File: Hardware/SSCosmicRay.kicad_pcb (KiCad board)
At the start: 2 copper layers, 80 x 50 mm, 139 parts, among them J2 USB_MINI, J3 CONN-9, SW1 PGM, SW2 RST, U1 MAX4477, U2 MAX4477, U3 MAX4477, U4 MAX4477, U5 MAX4477, U7 LTC3129-SOP, U8 AOZ1280, X1 8MHz

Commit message: Update components
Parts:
- removed D17: CDBA140, SODFL5126-N
- removed J2: USB_MINI, CONN-WURTH-651005136421
- removed R12, R18, R19: 10k, RESC1608-N
- removed SW1: PGM, SW-TL3315
- removed SW2: RST, SW-TL3315
- added J1: ICSP-CORTEX, CONN-TC-2030-NL, F.Cu at (219.5, 94.0)
- added U6: STM32L100RBT6, QFP50P1200X1200-64N, F.Cu at (231.0, 69.5)
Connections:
- C17 pad 2: GND -> (no net)
- C18 pad 1: +3.3V -> (no net)
- C18 pad 2: GND -> (no net)
- C20 pad 1: +3.3V -> (no net)
- C20 pad 2: GND -> (no net)
- C21 pad 2: GND -> (no net)
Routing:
- net /Processor/MCLR: track 15.2 -> 0.00 mm
- net GND: track 164.7 -> 151.4 mm, vias 56 -> 55
- net +3.3V: track 48.7 -> 35.8 mm
- net /Processor/PGM: track 10.2 -> 0.00 mm
- net (no net): track 10.1 -> 6.46 mm, vias 0 -> 1

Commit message: Processor support circuitry
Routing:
- net /Processor/A2: track 29.2 -> 4.41 mm
- net /Processor/A1: track 28.0 -> 4.53 mm
- net /Processor/OSC2: track 10.8 -> 0.00 mm
- net /Processor/OSC1: track 10.8 -> 0.00 mm
- net (no net): track 6.46 -> 0.00 mm, vias 1 -> 0
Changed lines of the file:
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@@
   (general
     (links 246)
-    (no_connects 15)
-    (area 126.949999 52.949999 207.050001 103.050001)
+    (no_connects 17)
+    (area 116.000001 48.04 238.500422 108.7)
     (thickness 1.6)
     (drawings 44)
-    (tracks 598)
+    (tracks 572)
     (zones 0)
     (modules 134)
@@
     (effects (font (size 1.5 1.5) (thickness 0.3)))
   )
-  (segment (start 184 76.67) (end 184 77.5) (width 0.2032) (layer F.Cu) (net 0))
-  (segment (start 183.2 78.3) (end 183.2 79) (width 0.2032) (layer F.Cu) (net 0))
-  (segment (start 184 77.5) (end 183.2 78.3) (width 0.2032) (layer F.Cu) (net 0))
-  (segment (start 184.8 76.67) (end 184.8 75.2) (width 0.2032) (layer F.Cu) (net 0))
-  (via (at 184.8 75.2) (size 0.889) (layers F.Cu B.Cu) (net 0))
-  (segment (start 184.8 76.67) (end 184.8 79) (width 0.2032) (layer F.Cu) (net 0))
   (segment (start 140.3 99) (end 141.5 99) (width 0.2032) (layer B.Cu) (net 1))
   (segment (start 141.5 99) (end 140.3 99) (width 0.2032) (layer F.Cu) (net 1))
@@
   (segment (start 166.2 91.6) (end 166.2 90) (width 0.2032) (layer F.Cu) (net 13))
   (segment (start 166.85 92.25) (end 166.2 91.6) (width 0.2032) (layer F.Cu) (net 13))
-  (segment (start 160 78) (end 179.7 78) (width 0.2032) (layer F.Cu) (net 14))
-  (segment (start 159.675 77.675) (end 160 78) (width 0.2032) (layer F.Cu) (net 14))
-  (segment (start 159.675 75.835) (end 159.675 77.675) (width 0.2032) (layer F.Cu) (net 14))
-  (segment (start 180 77.7) (end 180 76.67) (width 0.2032) (layer F.Cu) (net 14))
-  (segment (start 179.7 78) (end 180 77.7) (width 0.2032) (layer F.Cu) (net 14))
   (segment (start 159.2 73.5) (end 159.2 71.5) (width 0.2032) (layer F.Cu) (net 14))
   (segment (start 159.675 75.835) (end 159.675 74.675) (width 0.2032) (layer F.Cu) (net 14))
   (segment (start 159.2 74.2) (end 159.2 73.5) (width 0.2032) (layer F.Cu) (net 14))
   (segment (start 159.675 74.675) (end 159.2 74.2) (width 0.2032) (layer F.Cu) (net 14))
-  (segment (start 159.5 78.5) (end 180.5 78.5) (width 0.2032) (layer F.Cu) (net 15))
-  (segment (start 159.025 80.165) (end 159.025 78.975) (width 0.2032) (layer F.Cu) (net 15))
-  (segment (start 159.5 78.5) (end 159.025 78.975) (width 0.2032) (layer F.Cu) (net 15))
-  (segment (start 180.8 78.2) (end 180.8 76.67) (width 0.2032) (layer F.Cu) (net 15))
-  (segment (start 180.5 78.5) (end 180.8 78.2) (width 0.2032) (layer F.Cu) (net 15))
   (segment (start 159.2 82.5) (end 159.2 84.5) (width 0.2032) (layer F.Cu) (net 15))
   (segment (start 159.2 82.5) (end 159.2 81.7) (width 0.2032) (layer F.Cu) (net 15))
   (segment (start 159.025 81.525) (end 159.025 80.165) (width 0.2032) (layer F.Cu) (net 15))
   (segment (start 159.2 81.7) (end 159.025 81.525) (width 0.2032) (layer F.Cu) (net 15))
-  (segment (start 183.85 82) (end 185.6 82) (width 0.2032) (layer F.Cu) (net 16))
-  (segment (start 185.6 76.67) (end 185.6 82) (width 0.2032) (layer F.Cu) (net 16))
-  (segment (start 185.6 82) (end 185.6 84.8) (width 0.2032) (layer F.Cu) (net 16))
-  (segment (start 185.4 85) (end 184.8 85) (width 0.2032) (layer F.Cu) (net 16))
-  (segment (start 185.6 84.8) (end 185.4 85) (width 0.2032) (layer F.Cu) (net 16))
-  (segment (start 188.15 82) (end 186.4 82) (width 0.2032) (layer F.Cu) (net 17))
-  (segment (start 186.4 76.67) (end 186.4 82) (width 0.2032) (layer F.Cu) (net 17))
-  (segment (start 186.4 82) (end 186.4 84.8) (width 0.2032) (layer F.Cu) (net 17))
-  (segment (start 186.6 85) (end 187.2 85) (width 0.2032) (layer F.Cu) (net 17))
-  (segment (start 186.4 84.8) (end 186.6 85) (width 0.2032) (layer F.Cu) (net 17))
   (segment (start 167.84 95.75) (end 166.85 95.75) (width 0.2032) (layer F.Cu) (net 18))
   (via (at 166.45 95.25) (size 0.889) (layers F.Cu B.Cu) (net 18))

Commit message: Rough layout processor support components
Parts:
- added C47: 0.1uF, CAPC1608-N, F.Cu at (233.0, 77.5)
- added C48: 1uF, CAPC1608-N, F.Cu at (233.0, 79.5)
- added C49: 0.1uF, CAPC1608-N, F.Cu at (233.0, 81.5)
- added C50: 0.1uF, CAPC1608-N, F.Cu at (223.0, 73.0)
- added C51: 0.1uF, CAPC1608-N, F.Cu at (227.5, 77.5)
- added FB1: FERRITE, INDC1608-N, F.Cu at (236.0, 78.5)
- added R12: 10k, RESC1608-N, F.Cu at (221.0, 73.0)
- added R18: 10k, RESC1608-N, F.Cu at (227.5, 79.5)
- C17, C36, C39, C43, C44: footprint CAPC1608-N -> CAPC2012-N
- moved C17 57.0 mm to (238.5, 78.5), turned to 270 degrees
- moved C18 55.4 mm to (239.0, 72.5), turned to 270 degrees
- moved C21 52.3 mm to (227.5, 61.5), turned to 0 degrees
- moved C20 47.2 mm to (239.0, 66.0)
- moved J1 28.0 mm to (220.5, 66.0), turned to 270 degrees
- moved C43 0.50 mm to (173.0, 97.5)
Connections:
- C16 pad 1: /Processor/OSC1 -> /Processor/OSCI
- C17 pad 1: (no net) -> +3.3V
- C17 pad 2: (no net) -> GND
- C18 pad 1: (no net) -> +3.3V
- C18 pad 2: (no net) -> GND
- C19 pad 1: /Processor/OSC2 -> /Processor/OSCO
- C20 pad 1: (no net) -> +3.3V
- C20 pad 2: (no net) -> GND
- C21 pad 1: (no net) -> +3.3V
- C21 pad 2: (no net) -> GND
- J1 pad 2: (no net) -> /Processor/SWDIO
- J1 pad 3: (no net) -> /Processor/~RST
- J1 pad 4: (no net) -> /Processor/SWCLK
- U6 pad 1: (no net) -> /Processor/VLCD
- U6 pad 12: (no net) -> GND
- U6 pad 13: (no net) -> +3.3VADC
- U6 pad 18: (no net) -> GND
- U6 pad 19: (no net) -> +3.3V
- U6 pad 31: (no net) -> GND
- U6 pad 32: (no net) -> +3.3V
- U6 pad 46: (no net) -> /Processor/SWDIO
- U6 pad 47: (no net) -> GND
- U6 pad 48: (no net) -> +3.3V
- U6 pad 49: (no net) -> /Processor/SWCLK
- U6 pad 5: (no net) -> /Processor/OSCI
- U6 pad 6: (no net) -> /Processor/OSCO
- U6 pad 60: (no net) -> /Processor/BOOT
- U6 pad 63: (no net) -> GND
- U6 pad 64: (no net) -> +3.3V
- U6 pad 7: (no net) -> /Processor/~RST
- X1 pad 1: /Processor/OSC1 -> /Processor/OSCI
- X1 pad 2: /Processor/OSC2 -> /Processor/OSCO
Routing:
- net +12V: track 11.7 -> 10.4 mm, vias 5 -> 2

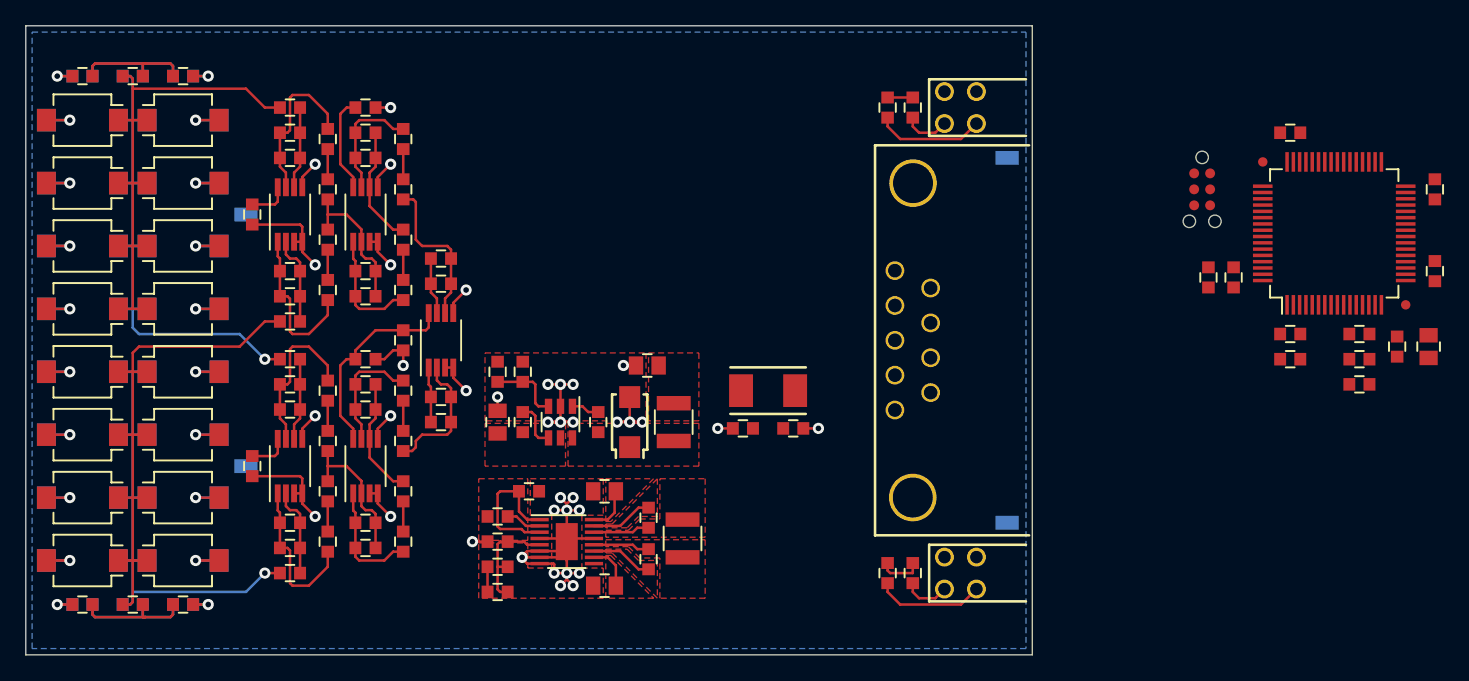
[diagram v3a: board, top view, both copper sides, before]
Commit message: Add threshold detector
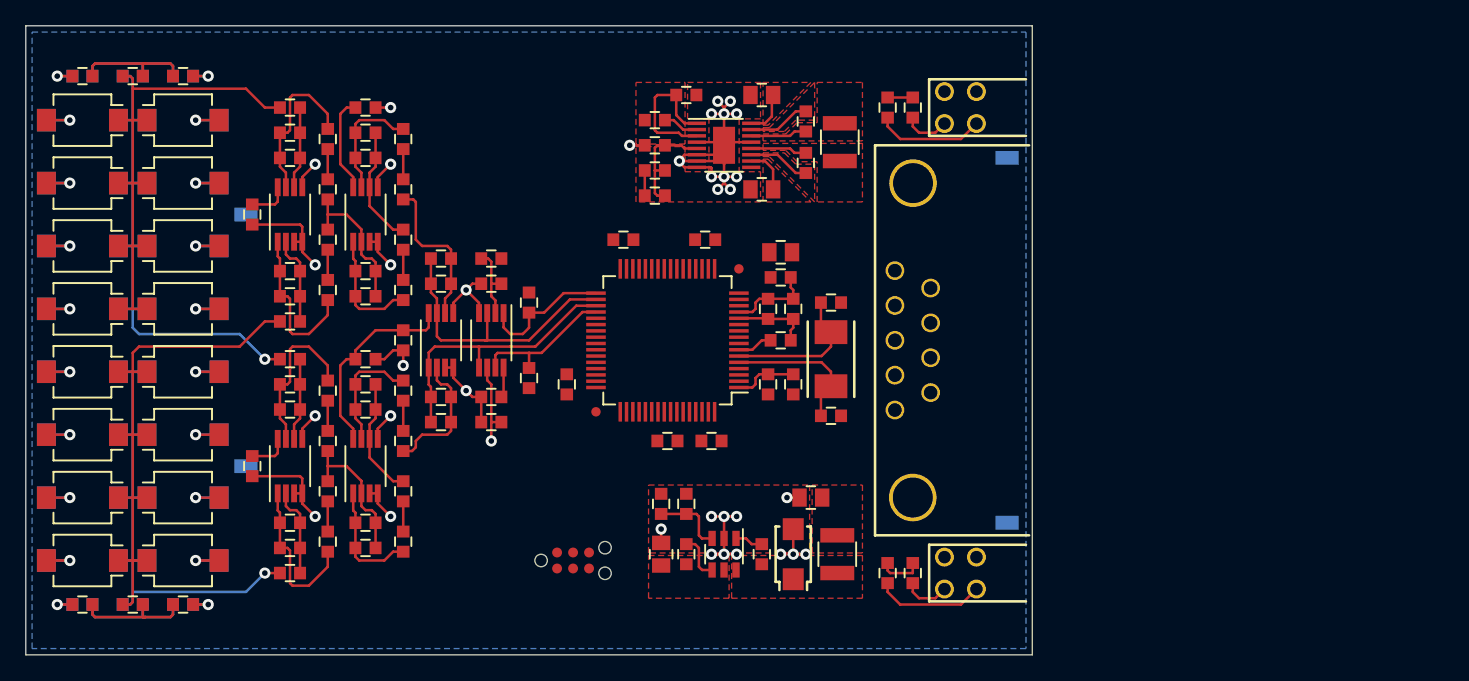
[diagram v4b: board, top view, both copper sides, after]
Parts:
- added C52: 0.1uF, CAPC1608-N, F.Cu at (164.0, 82.5)
- added C53: 0.1uF, CAPC1608-N, F.Cu at (164.0, 73.5)
- added C54: 0.1uF, CAPC1608-N, F.Cu at (164.0, 84.5)
- added R19: 10k, RESC1608-N, F.Cu at (164.0, 71.5)
- added R21: 10k, RESC1608-N, F.Cu at (167.0, 75.0)
- added R41: 10k, RESC1608-N, F.Cu at (167.0, 81.0)
- added U9: LM2903DT, SOP65P490-8N, F.Cu at (164.0, 78.0)
- moved C20 64.6 mm to (174.5, 70.0), turned to 0 degrees
- moved C21 60.9 mm to (170.0, 81.5), turned to 90 degrees
- moved J1 58.1 mm to (170.5, 95.5), turned to 0 degrees
- moved C18 58.1 mm to (181.0, 70.0), turned to 0 degrees
- moved U6 53.7 mm to (178.0, 78.0), turned to 90 degrees
- moved C17 52.0 mm to (187.0, 71.0), turned to 0 degrees
- moved FB1 49.3 mm to (187.0, 73.0), turned to 180 degrees
- moved C47 47.0 mm to (186.0, 75.5), turned to 270 degrees
- moved C49 46.1 mm to (187.0, 78.0)
- moved C48 45.2 mm to (188.0, 75.5), turned to 270 degrees
- moved R12 44.9 mm to (178.0, 86.0), turned to 0 degrees
- moved C50 43.5 mm to (181.5, 86.0), turned to 180 degrees
- moved C51 41.7 mm to (186.0, 81.5), turned to 270 degrees
- moved R18 39.6 mm to (188.0, 81.5), turned to 270 degrees
- moved C40 33.9 mm to (189.0, 63.9)
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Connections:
- J3 pad 7: (no net) -> /Processor/AOut
- U6 pad 20: (no net) -> /Processor/AOut
- U6 pad 21: (no net) -> /Processor/ATHR
- U6 pad 33: (no net) -> /Processor/DET1
- U6 pad 34: (no net) -> /Processor/A1
- U6 pad 35: (no net) -> /Processor/A2
- U6 pad 36: (no net) -> /Processor/DET2
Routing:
- net /Processor/A1: track 4.53 -> 22.8 mm
- net /Processor/A2: track 4.41 -> 22.1 mm
- net /Processor/THRSH: track 0.00 -> 12.7 mm, vias 0 -> 1
- net /Processor/DET2: track 0.00 -> 11.6 mm
- net /Processor/OSCO: track 0.00 -> 11.5 mm
- net /Processor/OSCI: track 0.00 -> 11.5 mm
- net GND: track 151.4 -> 162.2 mm, vias 55 -> 53
- net /Processor/DET1: track 0.00 -> 10.8 mm
- net +3.3VADC: track 0.00 -> 6.83 mm
- net /Processor/VLCD: track 0.00 -> 5.05 mm
- net /Processor/~RST: track 0.00 -> 2.83 mm
- net +3.3V: track 35.8 -> 38.2 mm

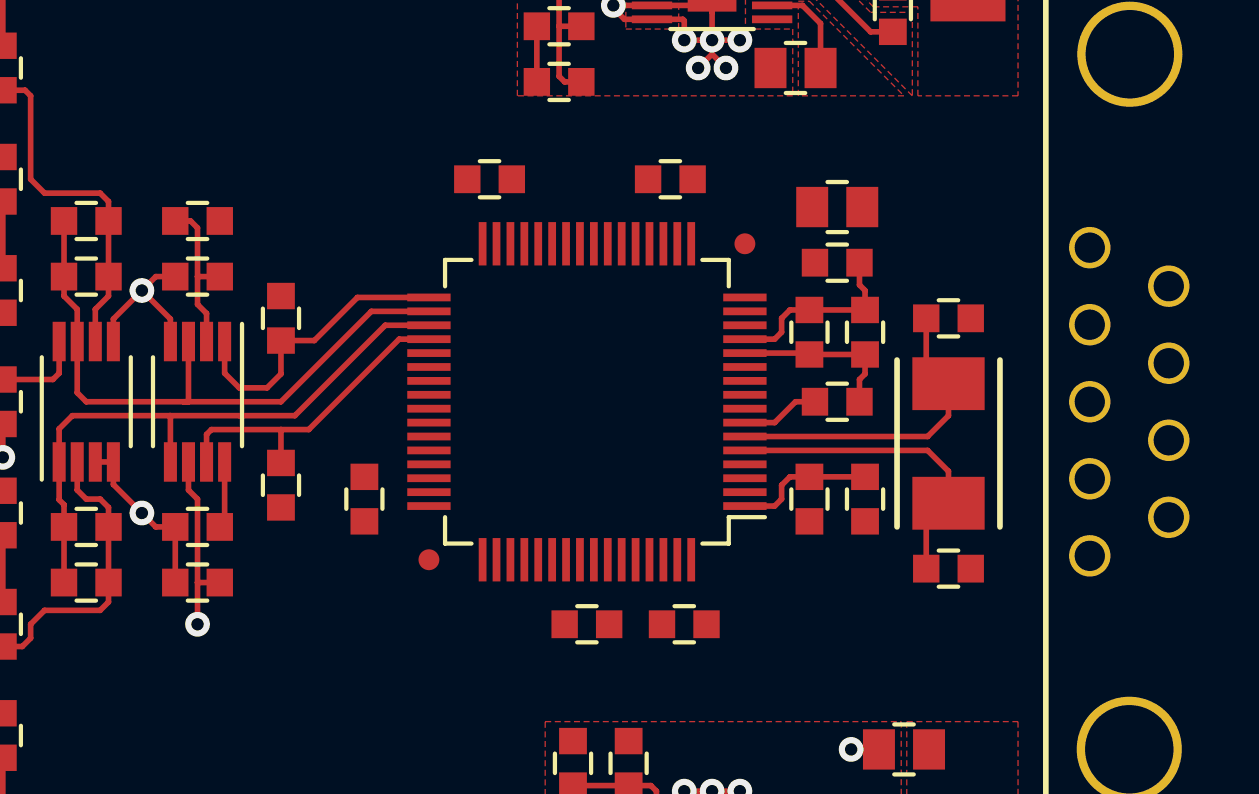
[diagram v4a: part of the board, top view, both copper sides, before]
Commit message: Serial IO connections
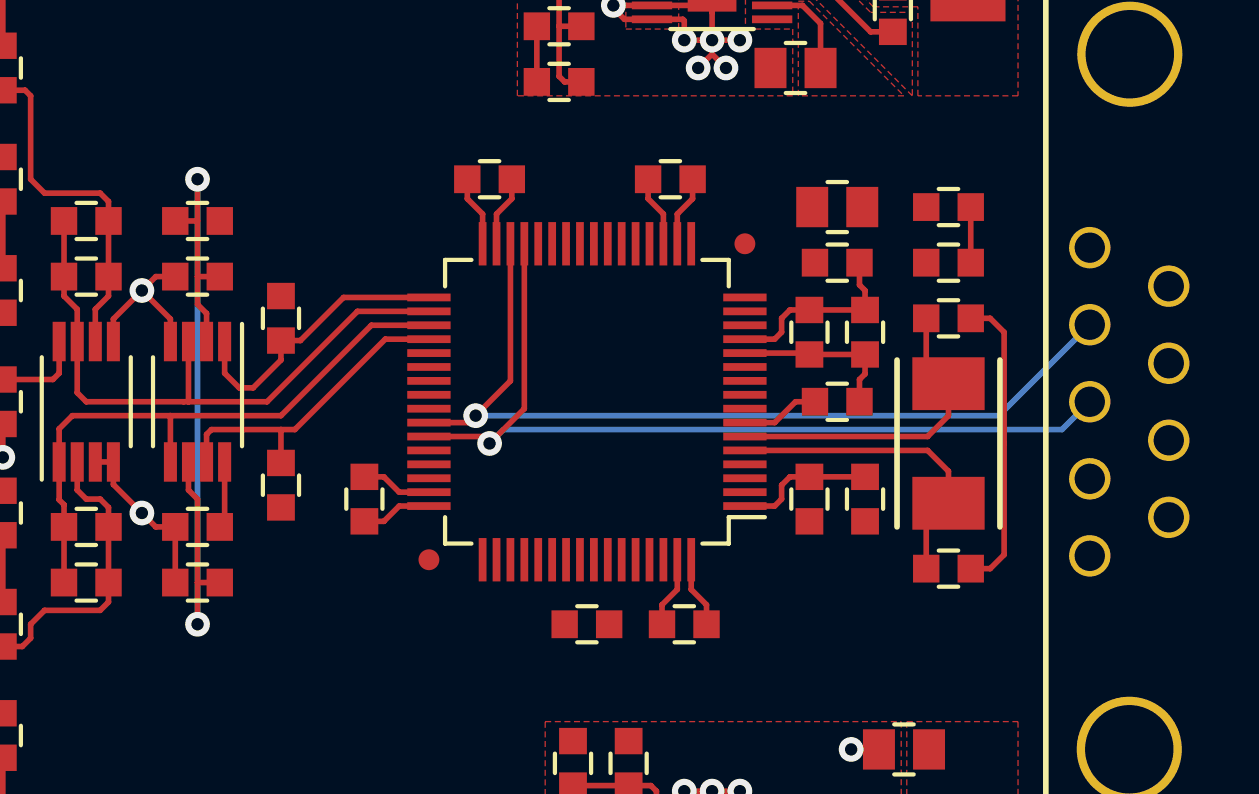
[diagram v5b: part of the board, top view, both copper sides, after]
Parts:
- added C55: 0.1uF, CAPC1608-N, F.Cu at (191.0, 73.0)
- added R42: 10k, RESC1608-N, F.Cu at (191.0, 71.0)
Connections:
- J3 pad 2: (no net) -> /Processor/DO
- J3 pad 3: (no net) -> /Processor/DI
- J3 pad 7: /Processor/AOut -> /Processor/AOUT
- U6 pad 20: /Processor/AOut -> /Processor/DAC
- U6 pad 29: (no net) -> /Processor/DI
- U6 pad 30: (no net) -> /Processor/DO
- U6 pad 42: (no net) -> /Processor/DO
- U6 pad 43: (no net) -> /Processor/DI
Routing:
- net /Processor/DI: track 0.00 -> 32.2 mm, vias 0 -> 1
- net /Processor/DO: track 0.00 -> 31.9 mm, vias 0 -> 1
- net GND: track 162.2 -> 183.2 mm
- net /Processor/THRSH: track 12.7 -> 30.3 mm, vias 1 -> 2
- net +3.3V: track 38.2 -> 48.4 mm
- net /Processor/AOUT: track 0.00 -> 2.00 mm

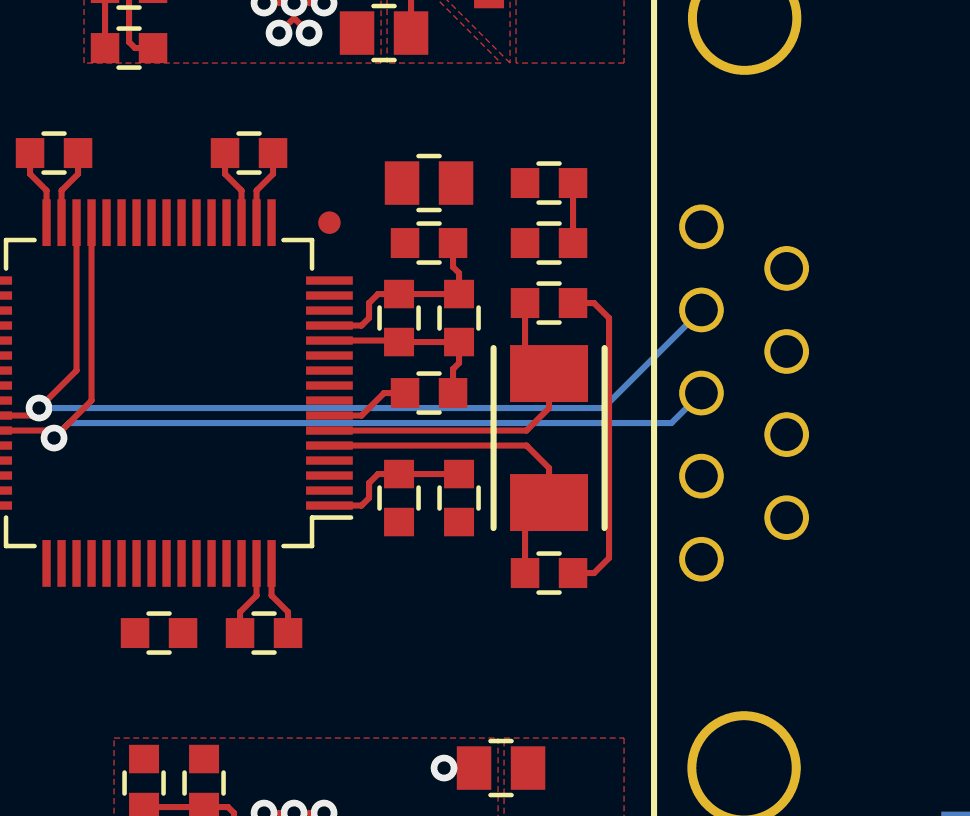
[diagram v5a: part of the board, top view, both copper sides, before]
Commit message: Change output pinout
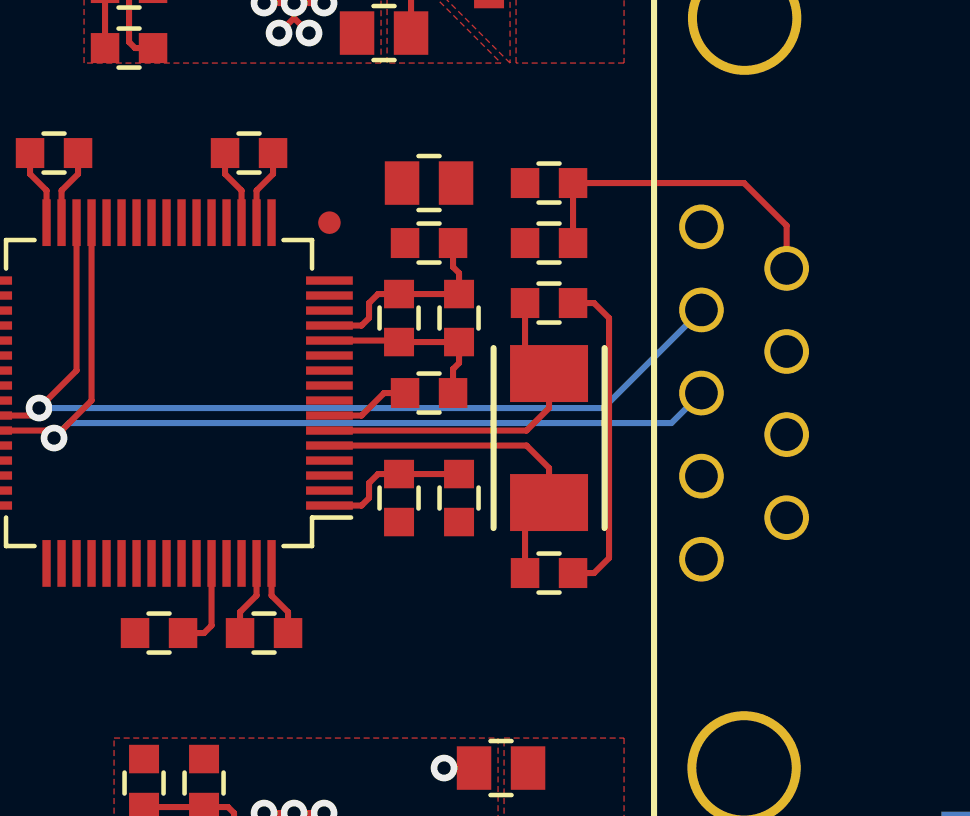
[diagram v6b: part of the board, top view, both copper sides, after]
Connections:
- J3 pad 6: (no net) -> /Processor/AOUT
- J3 pad 7: /Processor/AOUT -> (no net)
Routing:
- net /Processor/AOUT: track 2.00 -> 11.1 mm
- net /Processor/BOOT: track 0.00 -> 3.12 mm
